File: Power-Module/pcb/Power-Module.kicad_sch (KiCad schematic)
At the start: 5 parts, among them U4 TC2185-3.3VxCTTR

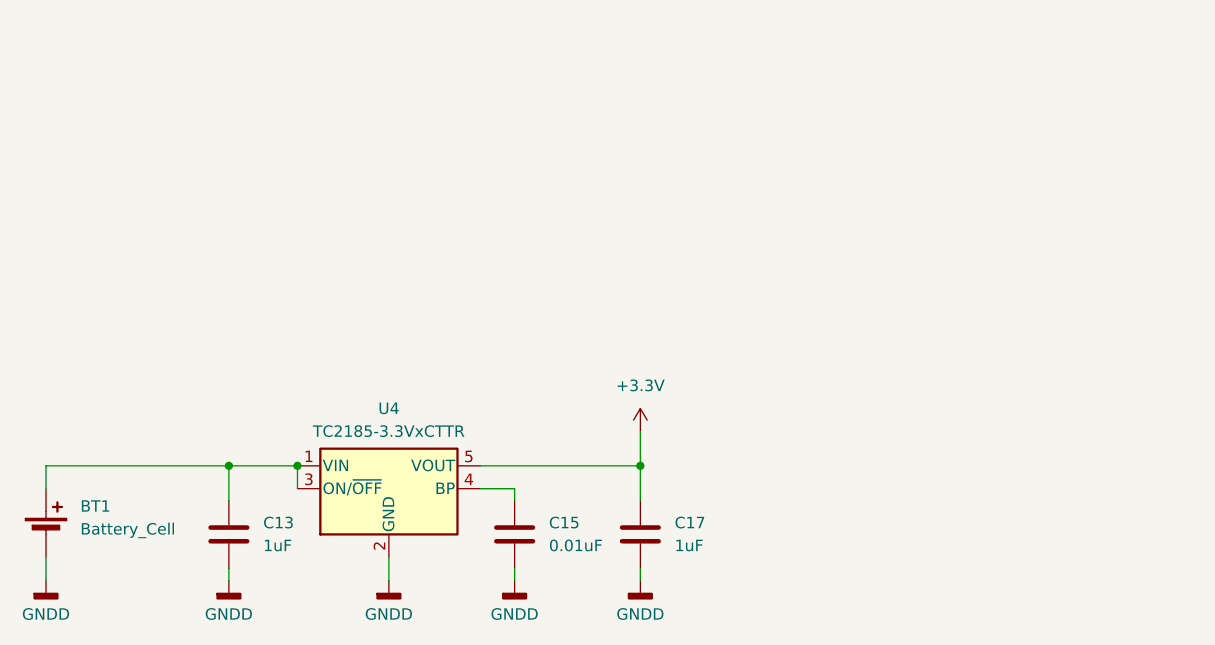
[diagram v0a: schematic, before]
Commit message: USB C breadboard supply passing DRC
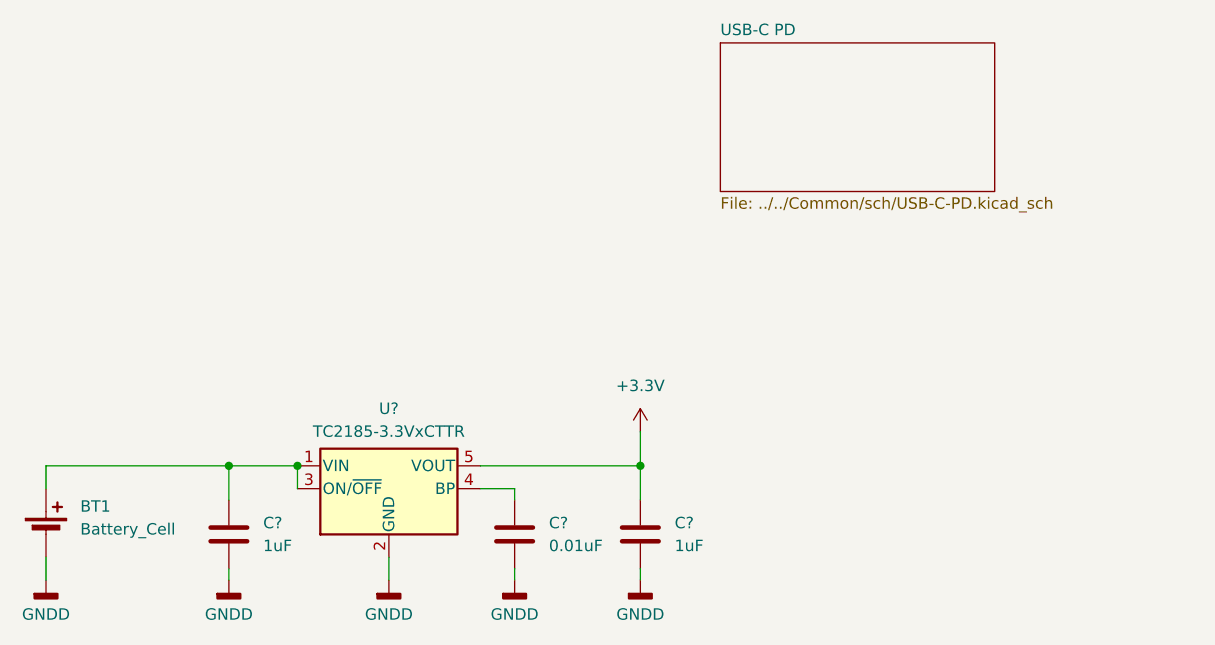
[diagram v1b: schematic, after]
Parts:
- renumbered C13 to C?, C15 to C?, C17 to C?, U4 to U?
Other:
- added sheet USB-C PD (../../Common/sch/USB-C-PD.kicad_sch)
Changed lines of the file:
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@@
 		(dnp no)
 		(fields_autoplaced yes)
-		(property "Reference" "#PWR033"
+		(property "Reference" "#PWR?"
 			(at 167.64 153.67 0)
 			(effects
@@
 		)
 		(instances
+			(project "Power-Module"
+				(path "/4a892dab-819f-4c9e-a23d-db3a8f679293"
+					(reference "#PWR?")
+					(unit 1)
+				)
+			)
 			(project ""
 				(path "/c41b490b-5ab6-4438-aea0-388670bb08f4/b5b03a48-538a-4431-9fe0-db318c963946"
@@
 		(dnp no)
 		(fields_autoplaced yes)
-		(property "Reference" "#PWR028"
+		(property "Reference" "#PWR?"
 			(at 139.7 153.67 0)
 			(effects
@@
 		)
 		(instances
+			(project "Power-Module"
+				(path "/4a892dab-819f-4c9e-a23d-db3a8f679293"
+					(reference "#PWR?")
+					(unit 1)
+				)
+			)
 			(project ""
 				(path "/c41b490b-5ab6-4438-aea0-388670bb08f4/b5b03a48-538a-4431-9fe0-db318c963946"
@@
 		(dnp no)
 		(fields_autoplaced yes)
-		(property "Reference" "#PWR032"
+		(property "Reference" "#PWR?"
 			(at 167.64 134.62 0)
 			(effects
@@
 		)
 		(instances
+			(project "Power-Module"
+				(path "/4a892dab-819f-4c9e-a23d-db3a8f679293"
+					(reference "#PWR?")
+					(unit 1)
+				)
+			)
 			(project ""
 				(path "/c41b490b-5ab6-4438-aea0-388670bb08f4/b5b03a48-538a-4431-9fe0-db318c963946"
@@
 		(dnp no)
 		(fields_autoplaced yes)
-		(property "Reference" "C13"
+		(property "Reference" "C?"
 			(at 125.73 140.9699 0)
 			(effects
@@
 		)
 		(instances
+			(project "Power-Module"
+				(path "/4a892dab-819f-4c9e-a23d-db3a8f679293"
+					(reference "C?")
+					(unit 1)
+				)
+			)
 			(project ""
 				(path "/c41b490b-5ab6-4438-aea0-388670bb08f4/b5b03a48-538a-4431-9fe0-db318c963946"
@@
 		(dnp no)
 		(fields_autoplaced yes)
-		(property "Reference" "#PWR027"
+		(property "Reference" "#PWR?"
 			(at 121.92 153.67 0)
 			(effects
@@
 		)
 		(instances
+			(project "Power-Module"
+				(path "/4a892dab-819f-4c9e-a23d-db3a8f679293"
+					(reference "#PWR?")
+					(unit 1)
+				)
+			)
 			(project ""
 				(path "/c41b490b-5ab6-4438-aea0-388670bb08f4/b5b03a48-538a-4431-9fe0-db318c963946"
@@
 		(dnp no)
 		(fields_autoplaced yes)
-		(property "Reference" "C15"
+		(property "Reference" "C?"
 			(at 157.48 140.9699 0)
 			(effects
@@
 		)
 		(instances
+			(project "Power-Module"
+				(path "/4a892dab-819f-4c9e-a23d-db3a8f679293"
+					(reference "C?")
+					(unit 1)
+				)
+			)
 			(project ""
 				(path "/c41b490b-5ab6-4438-aea0-388670bb08f4/b5b03a48-538a-4431-9fe0-db318c963946"
@@
 		(dnp no)
 		(fields_autoplaced yes)
-		(property "Reference" "C17"
+		(property "Reference" "C?"
 			(at 171.45 140.9699 0)
 			(effects
@@
 		)
 		(instances
+			(project "Power-Module"
+				(path "/4a892dab-819f-4c9e-a23d-db3a8f679293"
+					(reference "C?")
+					(unit 1)
+				)
+			)
 			(project "SRAD-Avionics"
 				(path "/c41b490b-5ab6-4438-aea0-388670bb08f4/b5b03a48-538a-4431-9fe0-db318c963946"
@@
 		(dnp no)
 		(fields_autoplaced yes)
-		(property "Reference" "#PWR030"
+		(property "Reference" "#PWR?"
 			(at 153.67 153.67 0)
 			(effects
@@
 		)
 		(instances
+			(project "Power-Module"
+				(path "/4a892dab-819f-4c9e-a23d-db3a8f679293"
+					(reference "#PWR?")
+					(unit 1)
+				)
+			)
 			(project ""
 				(path "/c41b490b-5ab6-4438-aea0-388670bb08f4/b5b03a48-538a-4431-9fe0-db318c963946"
@@
 		(dnp no)
 		(fields_autoplaced yes)
-		(property "Reference" "U4"
+		(property "Reference" "U?"
 			(at 139.7 128.27 0)
 			(effects
@@
 		)
 		(instances
+			(project "Power-Module"
+				(path "/4a892dab-819f-4c9e-a23d-db3a8f679293"
+					(reference "U?")
+					(unit 1)
+				)
+			)
 			(project ""
 				(path "/c41b490b-5ab6-4438-aea0-388670bb08f4/b5b03a48-538a-4431-9fe0-db318c963946"
@@
 				)
 			)
+		)
+	)
+	(sheet
+		(at 176.53 87.63)
+		(size 30.48 16.51)
+		(fields_autoplaced yes)
+		(stroke
+			(width 0.1524)
+			(type solid)
+		)
+		(fill
+			(color 0 0 0 0.0000)
+		)
+		(property "Sheetname" "USB-C PD"
+			(at 176.53 86.9184 0)
+			(effects
+				(font
+					(size 1.27 1.27)
+				)
+				(justify left bottom)
+			)
+		)
+		(property "Sheetfile" "../../Common/sch/USB-C-PD.kicad_sch"
+			(at 176.53 104.7246 0)
+			(effects
+				(font
+					(size 1.27 1.27)
+				)
+				(justify left top)
+			)
+		)
+		(instances
+			(project "Power-Module"
+				(path "/4a892dab-819f-4c9e-a23d-db3a8f679293"
+					(page "2")
+				)
+			)
